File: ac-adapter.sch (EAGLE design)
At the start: 88 parts, among them IC1 SSC3S900, IC2 TL431, Q1 300V 5A, Q2 300V 5A, Q3 TLP621-1, T1 COMMON_FILTER-SU10VFC, T2 TRANSFORMAER_FLYBACK-ETD34

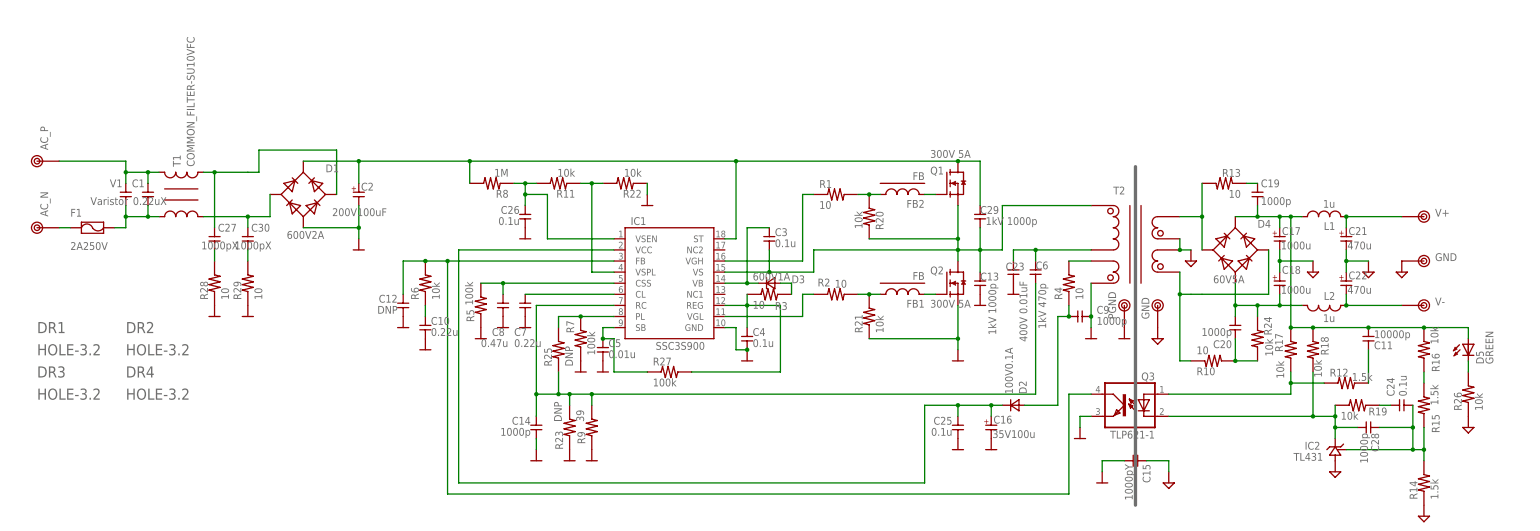
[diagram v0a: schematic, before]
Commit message: GaNに変更
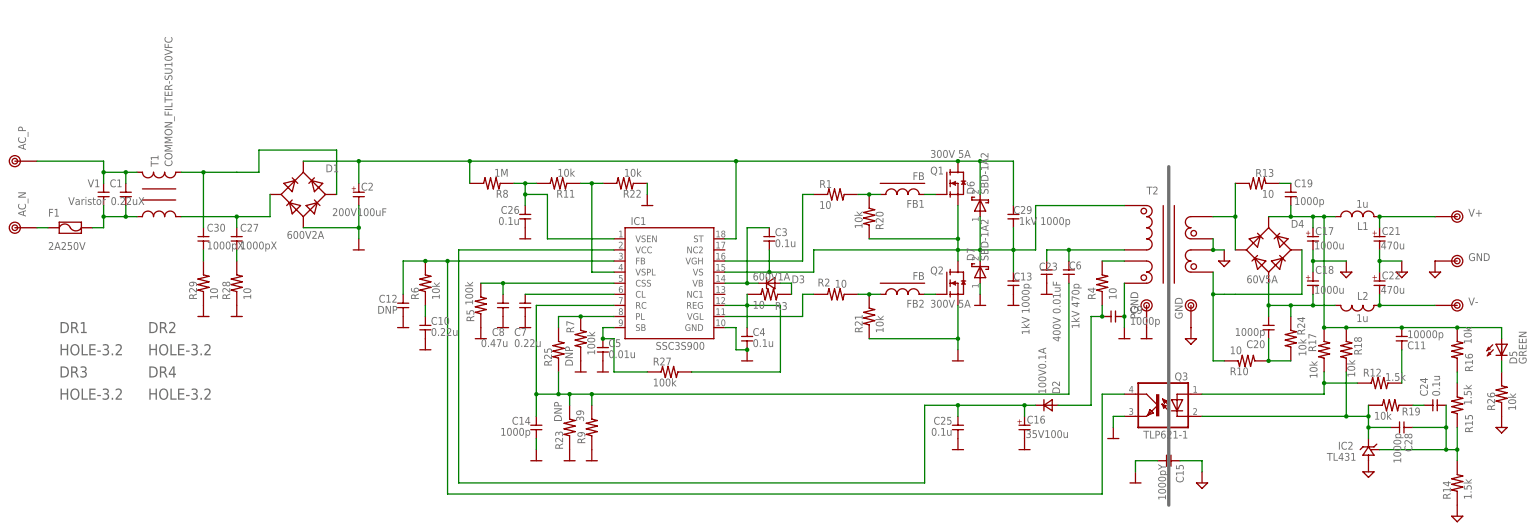
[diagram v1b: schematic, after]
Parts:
- added D6, D7: SBD-1A2, my_rcl:SBD-1A2
- Q1, Q2: device my_ic:NMOS-DFN -> my_ic:NMOS-GAN
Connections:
- net N$2: now also FB1.1; no longer FB2.1
- net N$39: now also Q1.G; no longer Q2.G
- net N$4: now also C30.1; no longer C27.1
- net N$41: now also Q2.G; no longer Q1.G
- net N$5: now also C27.1; no longer C30.1
- net N$9: now also FB2.1; no longer FB1.1
- net PGND: now also D7.A
- net SW: now also D6.A, D7.K
- net VH: now also D6.K
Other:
- moved on the sheet: C1, C11, C13, C15, C16, C17, C18, C19, C20, C21, C22, C23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
